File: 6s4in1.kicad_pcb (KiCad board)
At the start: 4 copper layers, 22.6 x 20 mm, 151 parts, among them P1 Pad, P10 Pad, P11 Pad, P12 Pad, P13 Pad, P14 Pad, P15 Pad, P16 Pad, P17 Pad, P18 Pad, P19 Pad, P2 Pad, P20 Pad, P21 Pad, P22 Pad, P3 Pad, P4 Pad, P5 Pad, P6 Pad, P7 Pad, P8 Pad, P9 Pad, Q1 NTLUD4C26N, Q10 NTLUD4C26N, Q11 NTLUD4C26N, Q12 NTLUD4C26N, Q2 NTLUD4C26N, Q3 NTLUD4C26N, Q4 NTLUD4C26N, Q5 NTLUD4C26N, Q6 NTLUD4C26N, Q7 NTLUD4C26N, Q8 NTLUD4C26N, Q9 NTLUD4C26N, U1 LM3480IM3-5.0, U10 TPS51604, U11 EFM8BB21-QFN20, U12 TPS51604, U13 TPS51604, U14 TPS51604, U15 EFM8BB21-QFN20, U16 TPS51604, U17 TPS51604, U18 TPS51604, U2 TLV70033, U3 EFM8BB21-QFN20, U4 TPS51604, U5 TPS51604, U6 TPS51604, U7 EFM8BB21-QFN20, U8 TPS51604, U9 TPS51604

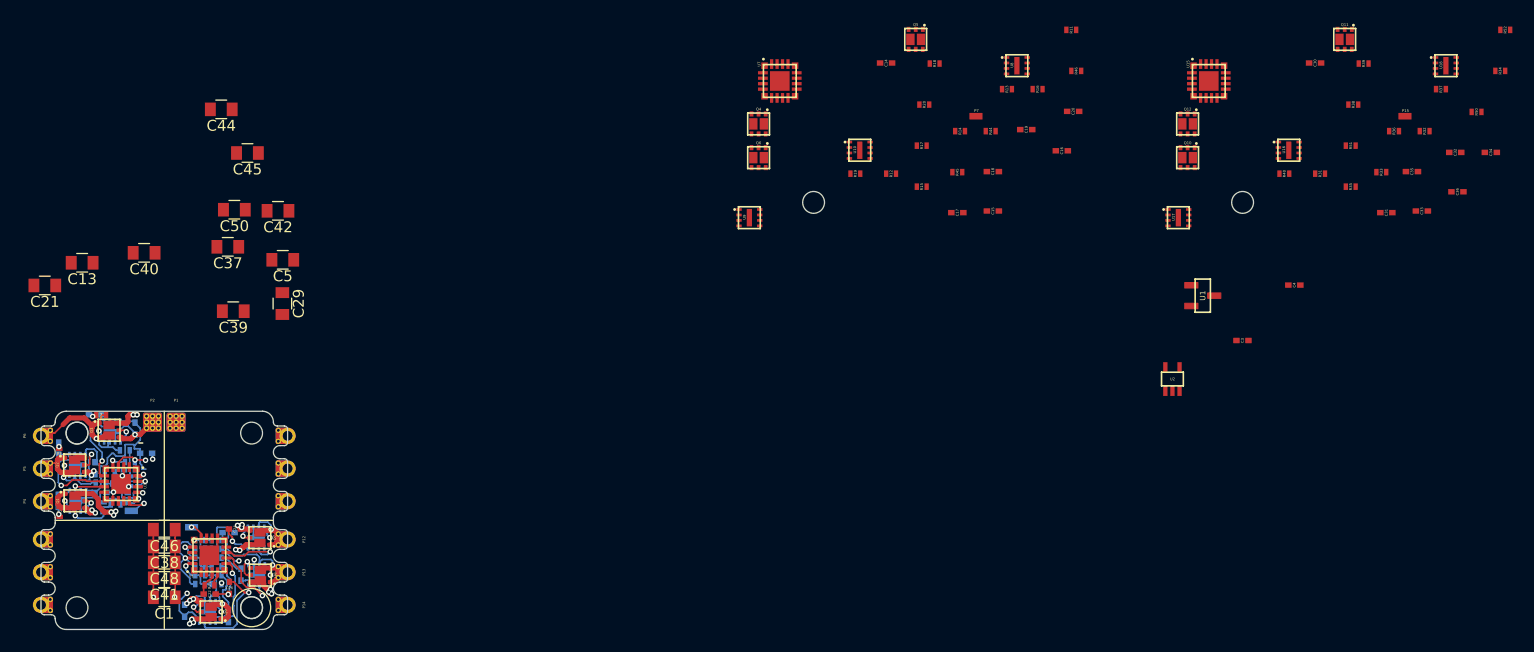
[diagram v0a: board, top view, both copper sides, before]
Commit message: Finished Routing
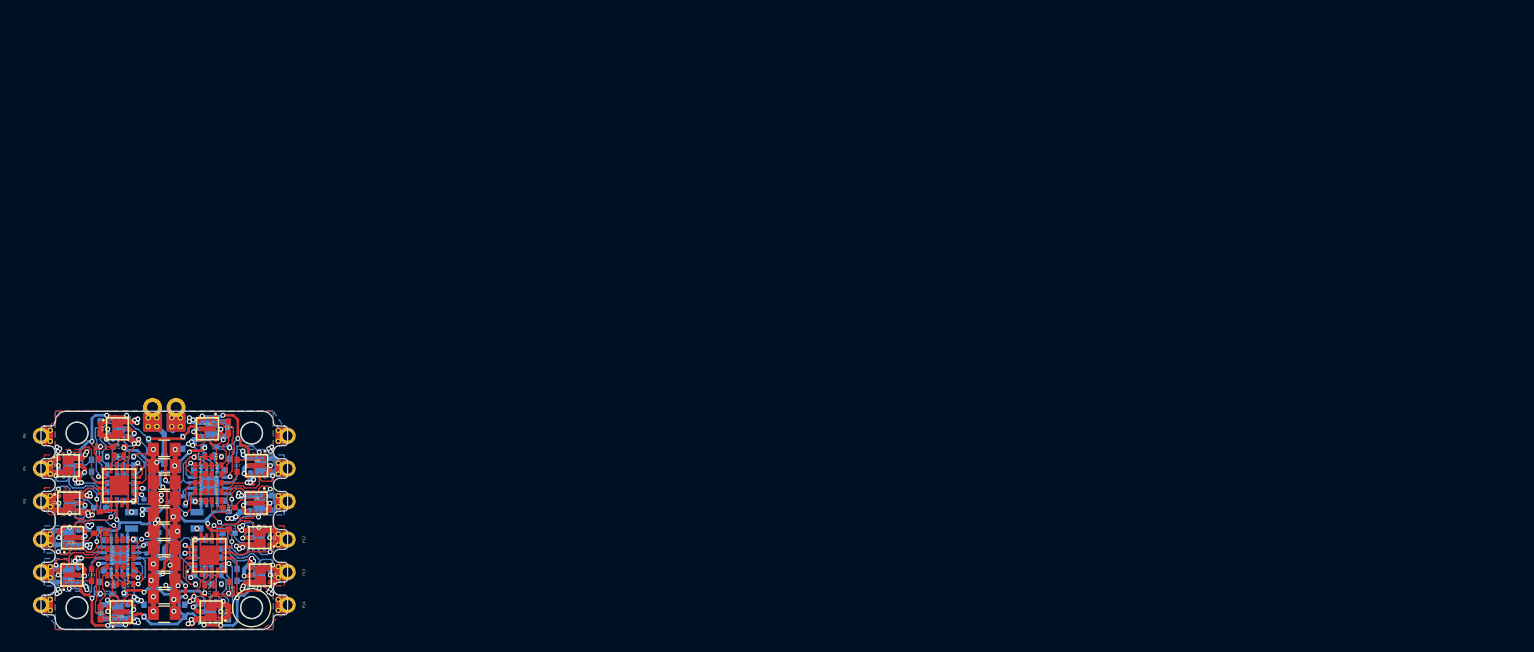
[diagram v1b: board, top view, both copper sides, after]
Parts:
- removed C44, C45, C46, C48, C50: 10uF, custom:C_0805
- added P23: Pad, custom:FlashPad, B.Cu at (28.1, 27.1)
- added P24: Pad, custom:FlashPad, B.Cu at (28.1, 28.1)
- added P25: Pad, custom:FlashPad, B.Cu at (31.7, 27.8)
- added P26: Pad, custom:FlashPad, B.Cu at (31.9, 28.6)
- added P27: Pad, custom:FlashPad, B.Cu at (31.9, 33.1)
- added P28: Pad, custom:FlashPad, B.Cu at (31.9, 32.3)
- added P29: Pad, custom:FlashPad, B.Cu at (28.4, 33.0)
- added P30: Pad, custom:FlashPad, B.Cu at (28.4, 32.1)
- C10, C6, C8, R1: moved to F.Cu
- C14, C16, C18, C20, C3, C30, C32, C34, C36, C4, P15, P20, P22, P7, Q10, Q11, Q12, Q4, Q5, Q6, R11, R2, R3, R31, R4, U1, U15, U2, U7: moved to B.Cu
- moved R52 137.4 mm to (25.2, 35.8), turned to 180 degrees
- moved R34 135.4 mm to (25.2, 35.0), turned to 180 degrees
- moved C34 133.7 mm to (24.0, 36.2), turned to 90 degrees
- moved U18 131.3 mm to (26.1, 38.4), turned to 90 degrees
- moved R50 131.3 mm to (25.2, 32.6), turned to 180 degrees
- moved C32 129.5 mm to (23.5, 30.8)
- moved R37 128.6 mm to (26.7, 35.8)
- moved Q11 126.9 mm to (21.2, 35.0), turned to 270 degrees
- moved C35 126.9 mm to (24.1, 38.5), turned to 270 degrees
- moved C33 126.4 mm to (23.3, 35.0), turned to 270 degrees
- moved C36 126.4 mm to (28.1, 38.3), turned to 270 degrees
- moved R32 126.0 mm to (25.2, 31.8), turned to 180 degrees
- moved P15 122.7 mm to (27.0, 30.8), turned to 180 degrees
- moved R36 122.7 mm to (26.7, 34.2)
- moved R39 121.9 mm to (26.7, 33.4)
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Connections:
- U11 pad 18: (no net) -> Net-(P27-Pad~)
- U15 pad 18: (no net) -> Net-(P29-Pad~)
- U3 pad 18: (no net) -> Net-(P23-Pad~)
- U7 pad 18: (no net) -> Net-(P25-Pad~)
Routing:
- net GND: track 52.6 -> 150.3 mm, vias 20 -> 56
- net 5V: track 39.5 -> 117.6 mm, vias 3 -> 24
- net VCC: track 25.5 -> 62.4 mm, vias 14 -> 54
- net 3.3V: track 6.54 -> 39.6 mm, vias 2 -> 8
- net /ESC_2/PHASE_B: track 0.00 -> 16.8 mm, vias 0 -> 1
- net /ESC_4/PHASE_B: track 0.00 -> 16.2 mm, vias 0 -> 1
- net /ESC_2/PHASEGND: track 0.00 -> 12.4 mm, vias 0 -> 2
- net /ESC_2/PHASE_C: track 0.00 -> 11.4 mm, vias 0 -> 2
- net /ESC_4/PHASEGND: track 0.00 -> 10.8 mm, vias 0 -> 2
- net /ESC_4/PHASE_C: track 0.00 -> 10.3 mm, vias 0 -> 2
- net /ESC_1/PHASEGND: track 4.79 -> 14.2 mm
- net /ESC_2/PHASE_A: track 0.00 -> 8.79 mm, vias 0 -> 1
- net /ESC_4/PHASE_A: track 0.00 -> 8.48 mm, vias 0 -> 1
- net /ESC_2/PWM_A: track 0.00 -> 7.82 mm, vias 0 -> 1
- net /ESC_4/PWM_A: track 0.00 -> 7.71 mm, vias 0 -> 1
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- added copper zone on F.Cu, net /ESC_1/PHASE_A
- added copper zone on F.Cu, net /ESC_1/PHASE_B
- added copper zone on F.Cu, net /ESC_1/PHASE_C
- added copper zone on B.Cu, net /ESC_2/PHASE_A
- added copper zone on B.Cu, net /ESC_2/PHASE_B
- added copper zone on B.Cu, net /ESC_2/PHASE_C
- added copper zone on F.Cu, net /ESC_3/PHASE_A
- added copper zone on F.Cu, net /ESC_3/PHASE_B
- added copper zone on F.Cu, net /ESC_3/PHASE_C
- added copper zone on B.Cu, net /ESC_4/PHASE_A
- added copper zone on B.Cu, net /ESC_4/PHASE_B
- added copper zone on B.Cu, net /ESC_4/PHASE_C
- added copper zone on B.Cu, net GND
- added copper zone on F.Cu, net GND
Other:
- net class Default: clearance 0.1524 -> 0.127; trace_width 0.1524 -> 0.127; via_dia 0.508 -> 0.4572
- rule trace_clearance: 0.1524 -> 0.127
- rule trace_min: 0.1524 -> 0.127
- rule via_min_size: 0.508 -> 0.4572
- board text removed: "-"

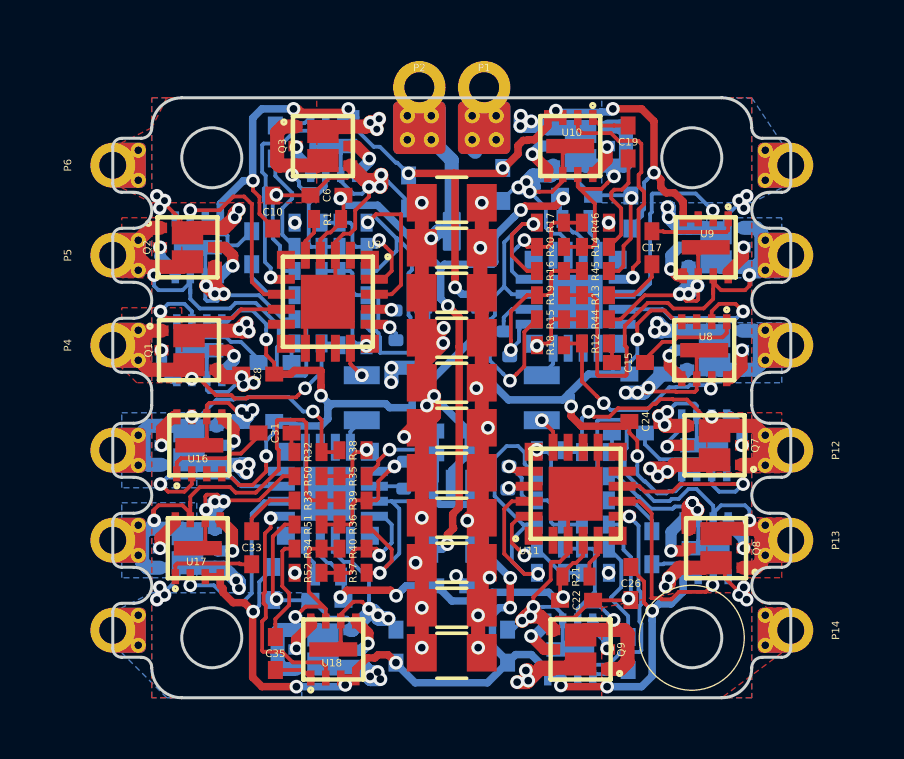
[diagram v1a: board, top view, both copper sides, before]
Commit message: Added Tx/Rx labels and +/- labels
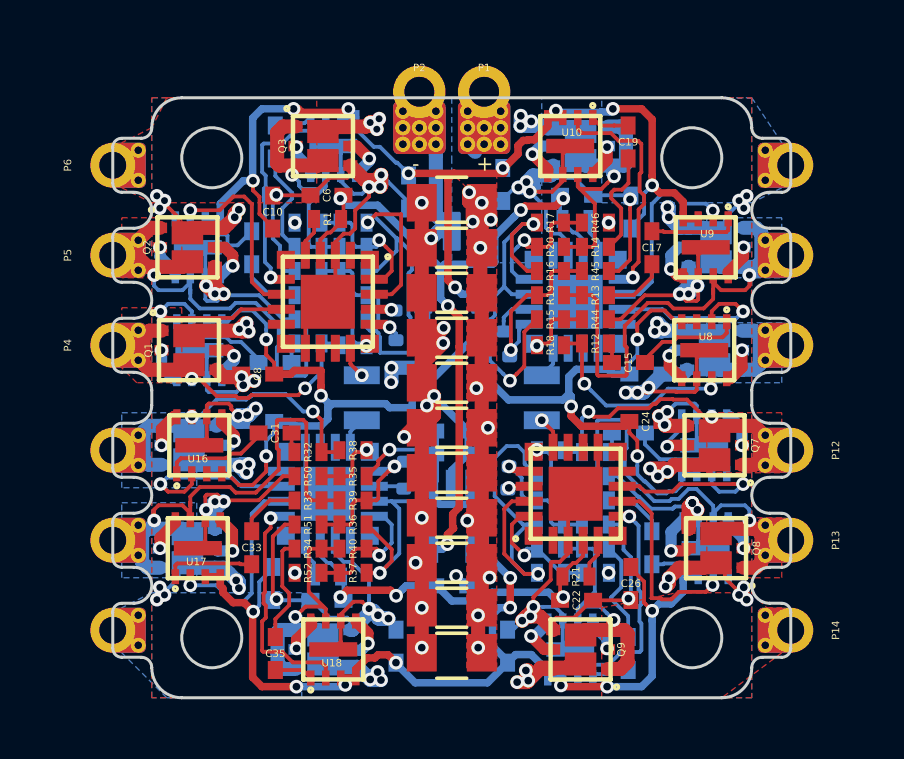
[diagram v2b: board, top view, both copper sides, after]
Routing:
- net VCC: track 62.4 -> 65.2 mm, vias 54 -> 57
- added copper zone on B.Cu, net VCC
- added copper zone on F.Cu, net VCC
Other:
- board text added: "+"
- board text added: "-"
- board text added: "R"
- board text added: "T"

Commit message: cleaning up for public
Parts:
- R12, R13, R14, R2, R22, R23, R24, R3, R32, R33, R34, R4: value 3 -> 1
